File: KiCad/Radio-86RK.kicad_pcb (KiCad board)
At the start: 2 copper layers, 266.7 x 203.2 mm, 188 parts, among them J1 Video, J2 5V, J3 Power, J4 Cassette, J5 Serial, J6 Parallel, Q1 2N3904, Q2 2N3904, SW1 FF, SW10 ВК CR, SW11 ЗБ DEL, SW12 LEFT, SW13 UP, SW14 RIGHT, SW15 DOWN, SW16 0, SW17 1 !, SW18 2 ", SW19 3 #, SW2 СТР CLS, SW20 4 $, SW21 5 %, SW22 6 &, SW23 7 ', SW24 8 (, SW25 9 ), SW26 : *, SW27 ; +, SW28 , <, SW29 - =, SW3 АР2 ESC, SW30 . >, SW31 / ?, SW32 Ю @, SW33 А A, SW34 Б B, SW35 Ц C, SW36 Д D, SW37 Е E, SW38 Ф F, SW39 Г G, SW4 F1, SW40 Х H, SW41 И I, SW42 Й J, SW43 К K, SW44 Л L, SW45 М M, SW46 Н N, SW47 О O, SW48 П P, SW49 Я Q, SW5 F2, SW50 Р R, SW51 С S, SW52 Т T, SW53 У U, SW54 Ж V, SW55 В W, SW56 X Ь, SW57 Ы Y, SW58 З Z, SW59 Ш [, SW6 F3, SW60 Э \, SW61 Щ ], SW62 Ч ^, SW63 SPACE, SW64 УС CTRL, SW65 CC GRAPH, SW66 RUS/LAT, SW67 Reset, SW7 F4, SW8 ТАБ TAB, SW9 ПС LF, U1 8080A/КР580ВМ80А, U10 2716/КР573РФ5, U11 2716/КР573РФ5, U12 74LS373/К555ИР22, U13 74198/К155ИР13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

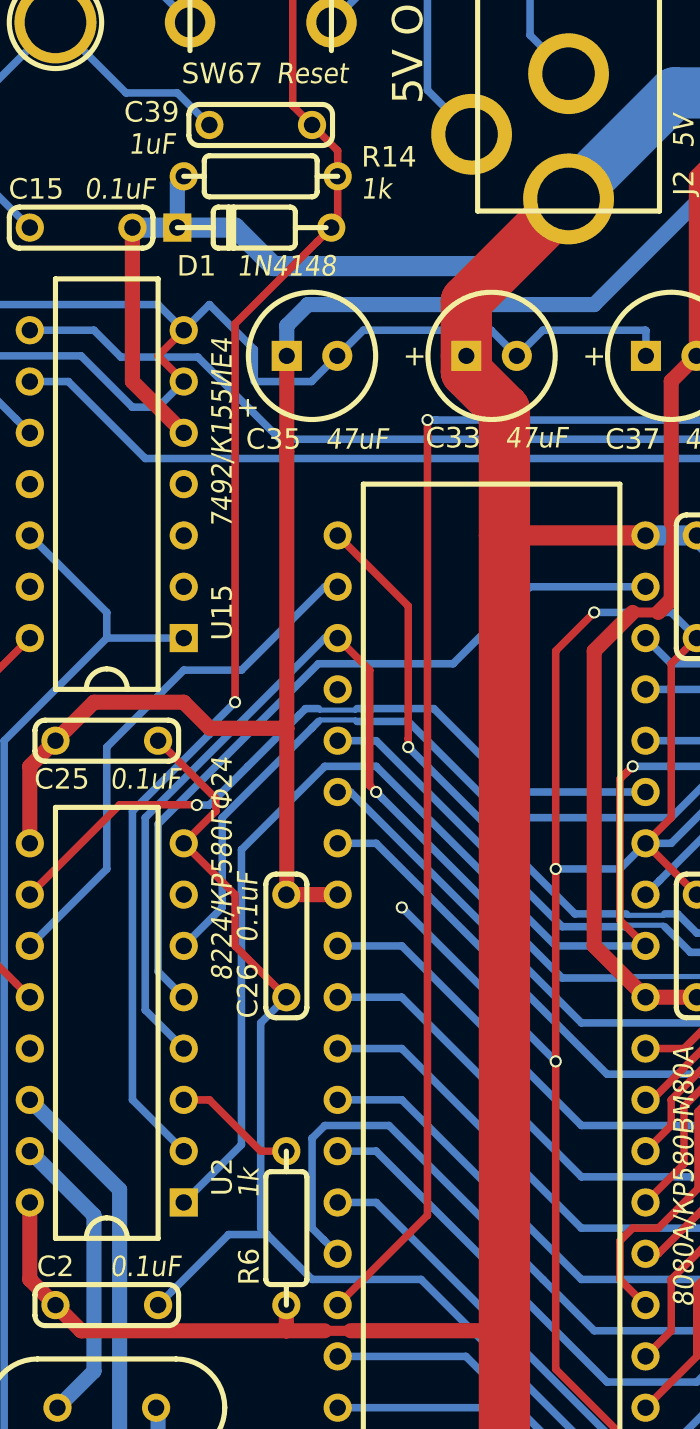
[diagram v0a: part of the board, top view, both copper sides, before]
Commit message: Use DS1233 for reset
Signed-off-by: Sergey Kiselev <skiselev@gmail.com>
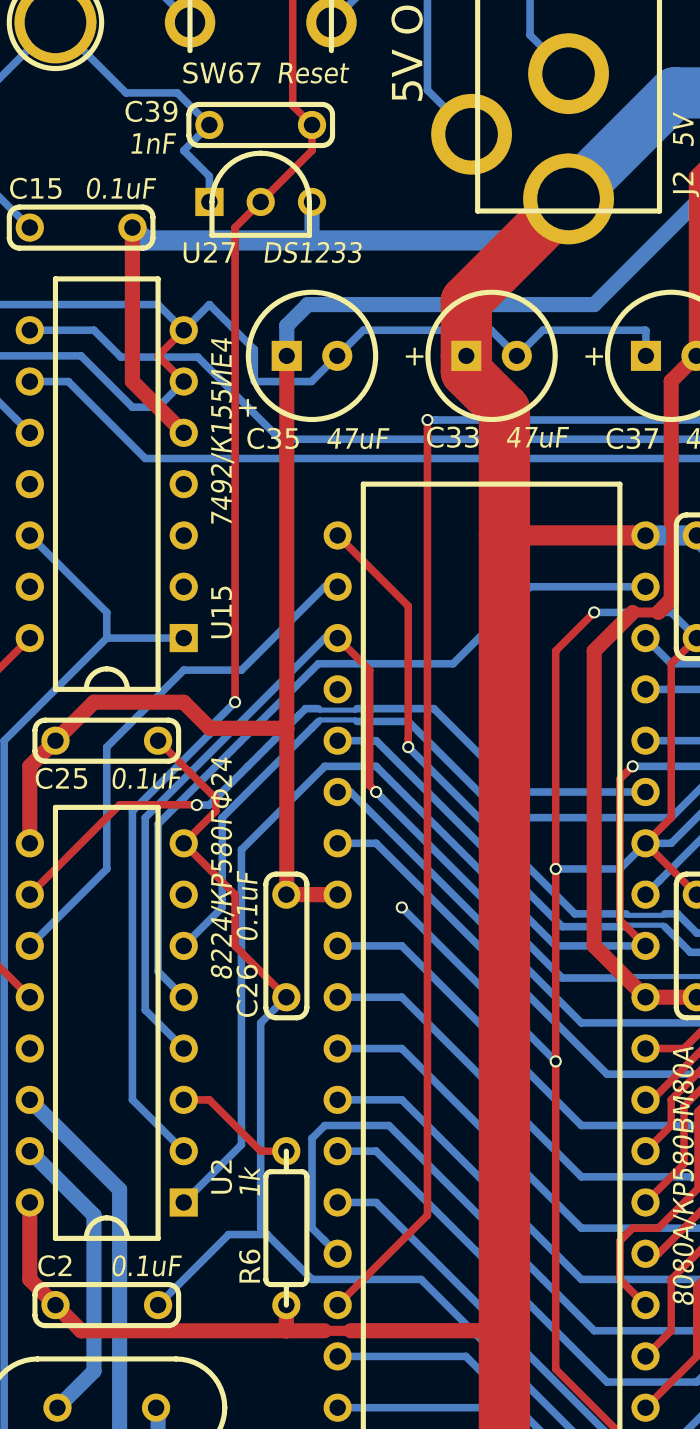
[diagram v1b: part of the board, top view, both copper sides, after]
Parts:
- removed D1: 1N4148, My_Components:Diode_762
- removed R14: 1k, My_Components:Res_762
- added U27: DS1233, My_Components:Transistor_TO92_EBC_254, F.Cu at (21.6, 20.3)
- C39: value 1uF -> 1nF
- turned R6 to 270 degrees
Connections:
- R6 pad 1: VCC -> Net-(R6-Pad1)
- R6 pad 2: Net-(R6-Pad2) -> VCC
- U2 pad 3: Net-(R6-Pad2) -> Net-(R6-Pad1)
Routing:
- net Net-(R6-Pad2): track 6.13 -> 0.00 mm
- net Net-(R6-Pad1): track 0.00 -> 6.13 mm
- net GND: track 2983.2 -> 2988.1 mm
- net VCC: track 1026.8 -> 1025.0 mm
- net Net-(C39-Pad1): track 64.8 -> 63.8 mm

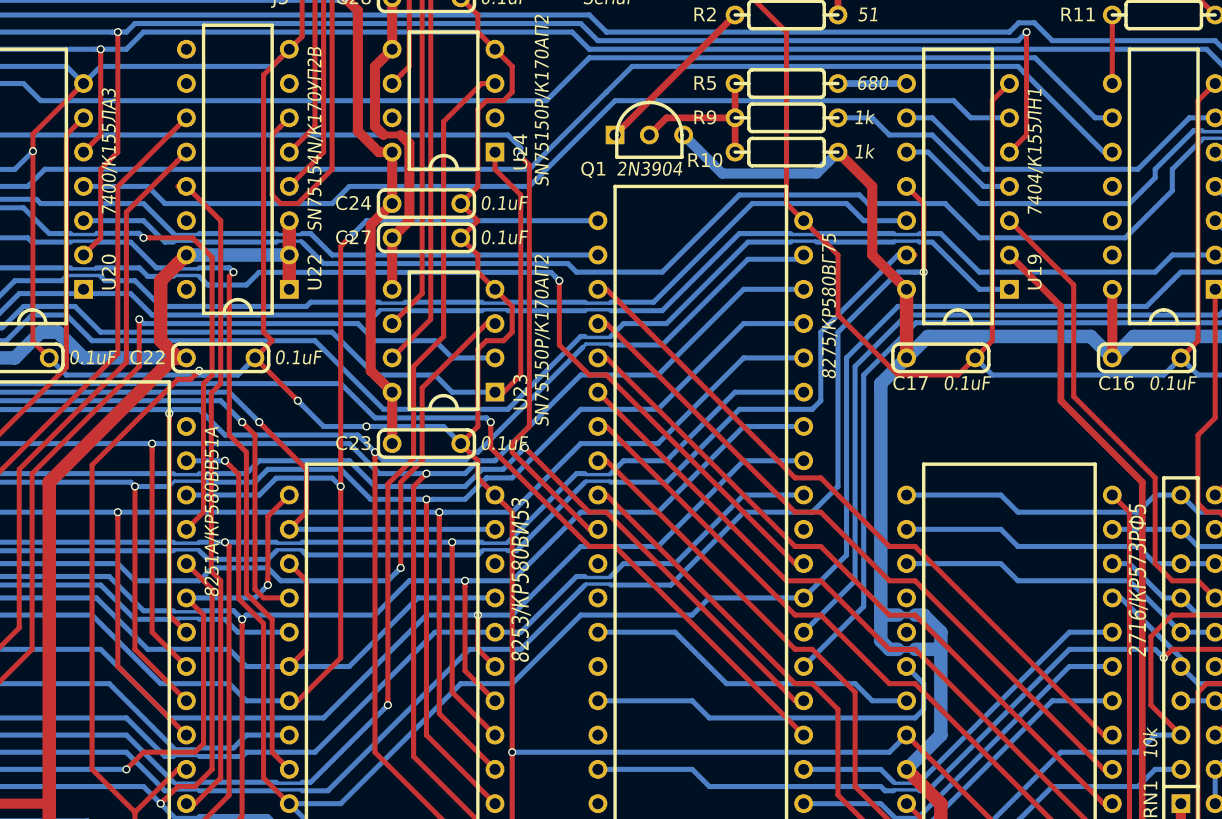
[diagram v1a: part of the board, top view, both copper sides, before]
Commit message: Implement inverse video
Signed-off-by: Sergey Kiselev <skiselev@gmail.com>
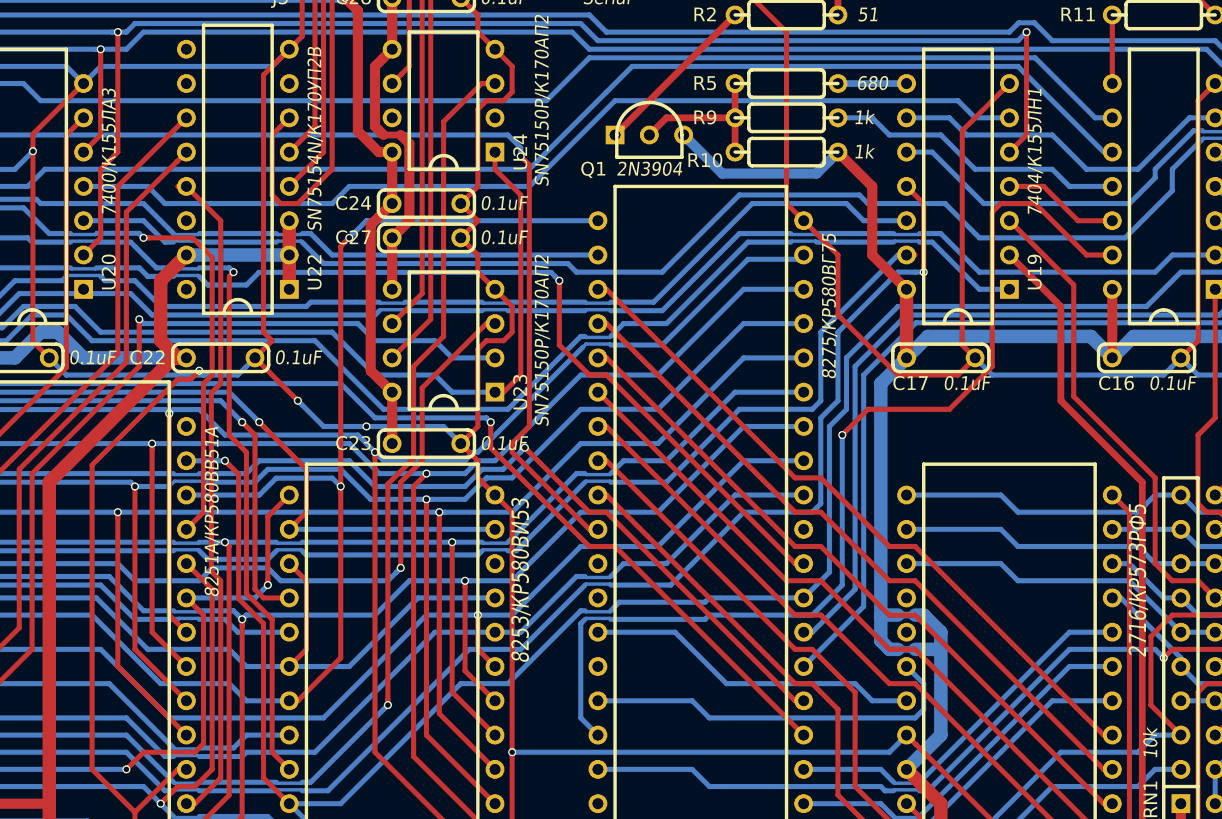
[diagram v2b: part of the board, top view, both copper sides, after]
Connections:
- U16 pad 11: Net-(U16-Pad11) -> Net-(R9-Pad2)
- U19 pad 4: Net-(R9-Pad2) -> Net-(U16-Pad12)
- U8 pad 36: Net-(U8-Pad36) -> Net-(U16-Pad13)
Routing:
- net Net-(U16-Pad13): track 0.00 -> 75.9 mm, vias 0 -> 1
- net Net-(U16-Pad12): track 0.00 -> 8.67 mm
- net Net-(R9-Pad2): track 14.8 -> 22.4 mm
- net GND: track 2988.1 -> 2988.9 mm

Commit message: Update design files to v1.1
Signed-off-by: Sergey Kiselev <skiselev@gmail.com>
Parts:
- removed the C39 at (21.6, 16.5)
- added C43: 1nF, My_Components:Cap_Cer_508, F.Cu at (21.6, 16.5)
- renumbered C40 to C39, C41 to C40, C42 to C41, C43 to C42, D2 to D1, D11 to D10, D12 to D11, D3 to D2, D4 to D3, D5 to D4, D6 to D5, D7 to D6, D8 to D7, D9 to D8, D10 to D9, R15 to R14, R16 to R15
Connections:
- D10 pad 2: /Keyboard/D11+ -> /Keyboard/D10+
- D11 pad 2: /Keyboard/D12+ -> /Keyboard/D11+
- R12 pad 2: /Keyboard/D11+ -> /Keyboard/D10+
- R13 pad 2: /Keyboard/D12+ -> /Keyboard/D11+
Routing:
- net /Keyboard/D10+: track 0.00 -> 15.0 mm
- net /Keyboard/D12+: track 8.30 -> 0.00 mm
- net /Keyboard/D11+: track 15.0 -> 8.30 mm
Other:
- board text added: "M<Address> - Modify memory content T<Start_Address>,<End_Address>,<Destination_Start_Address> - Copy memory block to destination C<Start_Address>,<End_Address>,<Destination_Start_Address> - Compare memory block with destination S<Start_Address>,<End_Address>,<Value> - Search memory for a value"
- board text added: "R<ROM_Start_Address>,<ROM_End_Address>,<Destination_Start_Address> - Read from ROM connected to Parallel interface to memory Monitor Commands - Run Control and Registers: G<Start_Address>[,End_Address] - Run code, optionally stop at the specified address X - Display and modify registers"
- board text added: "Radio-86RK - Version 1.1 PCB Layout - Copyright (C) Sergey Kiselev github.com/skiselev/radio-86rk"
- board text removed: "Monitor Commands - Run Control and Registers: G<Start_Address>[,End_Address] - Run code, optionally stop at the specified address X - Display and modify registers"
- board text removed: "Radio-86RK - Version 1.0 PCB Layout - Copyright (C) Sergey Kiselev github.com/skiselev/radio-86rk"
- board text removed: "T<Start_Address>,<End_Address>,<Destination_Start_Address> - Copy memory block to destination C<Start_Address>,<End_Address>,<Destination_Start_Address> - Compare memory block with destination S<Start_Address>,<End_Address>,<Value> - Search memory for a value R<ROM_Start_Address>,<ROM_End_Address>,<Destination_Start_Address> - Read from ROM connected to Parallel interface to memory"

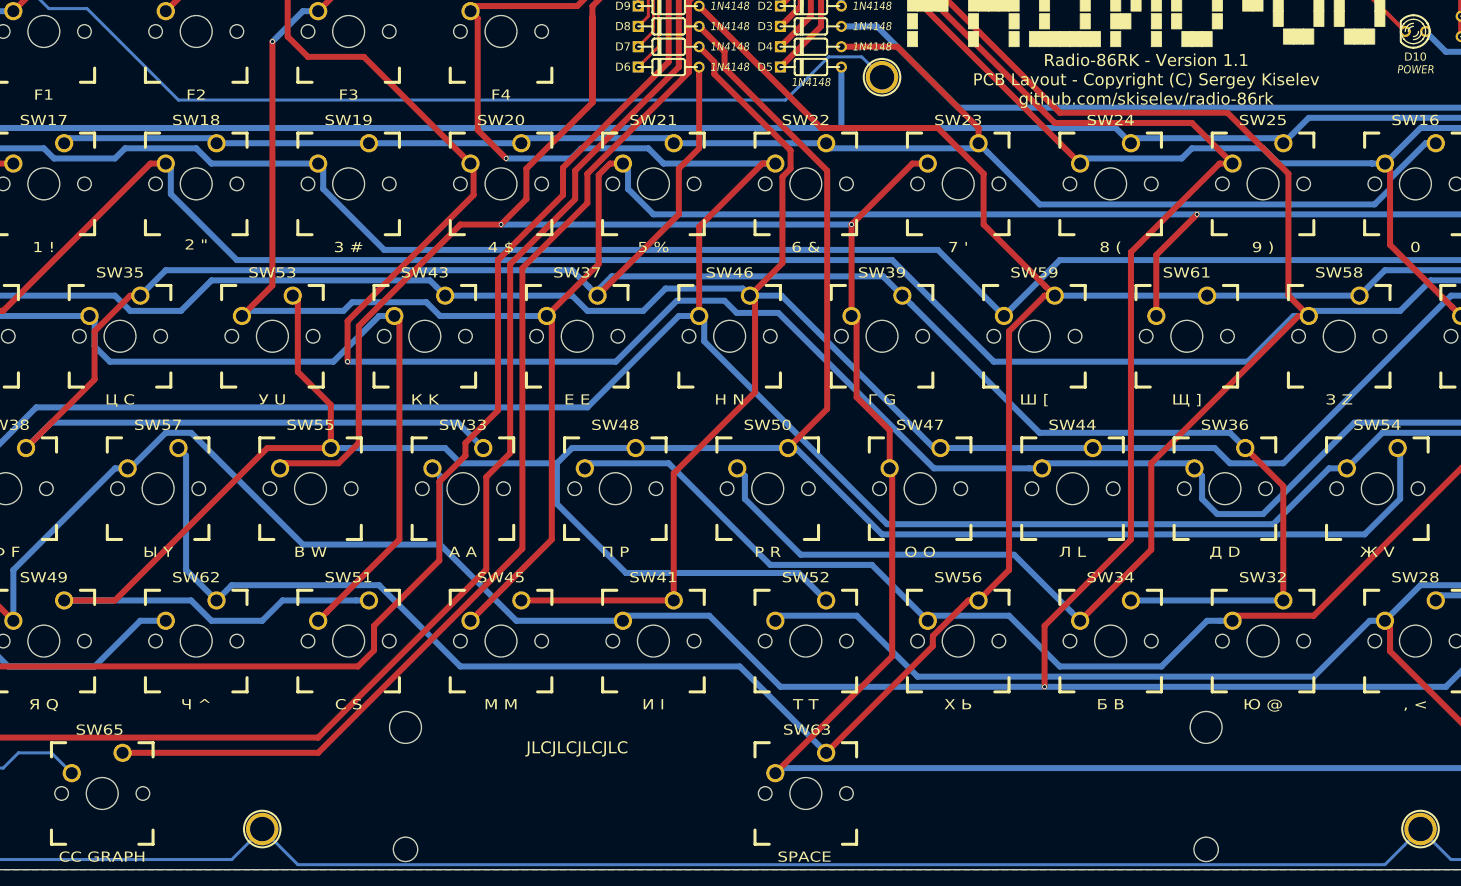
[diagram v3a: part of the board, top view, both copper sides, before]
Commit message: Fix issues on the front silkscreen
Signed-off-by: Sergey Kiselev <skiselev@gmail.com>
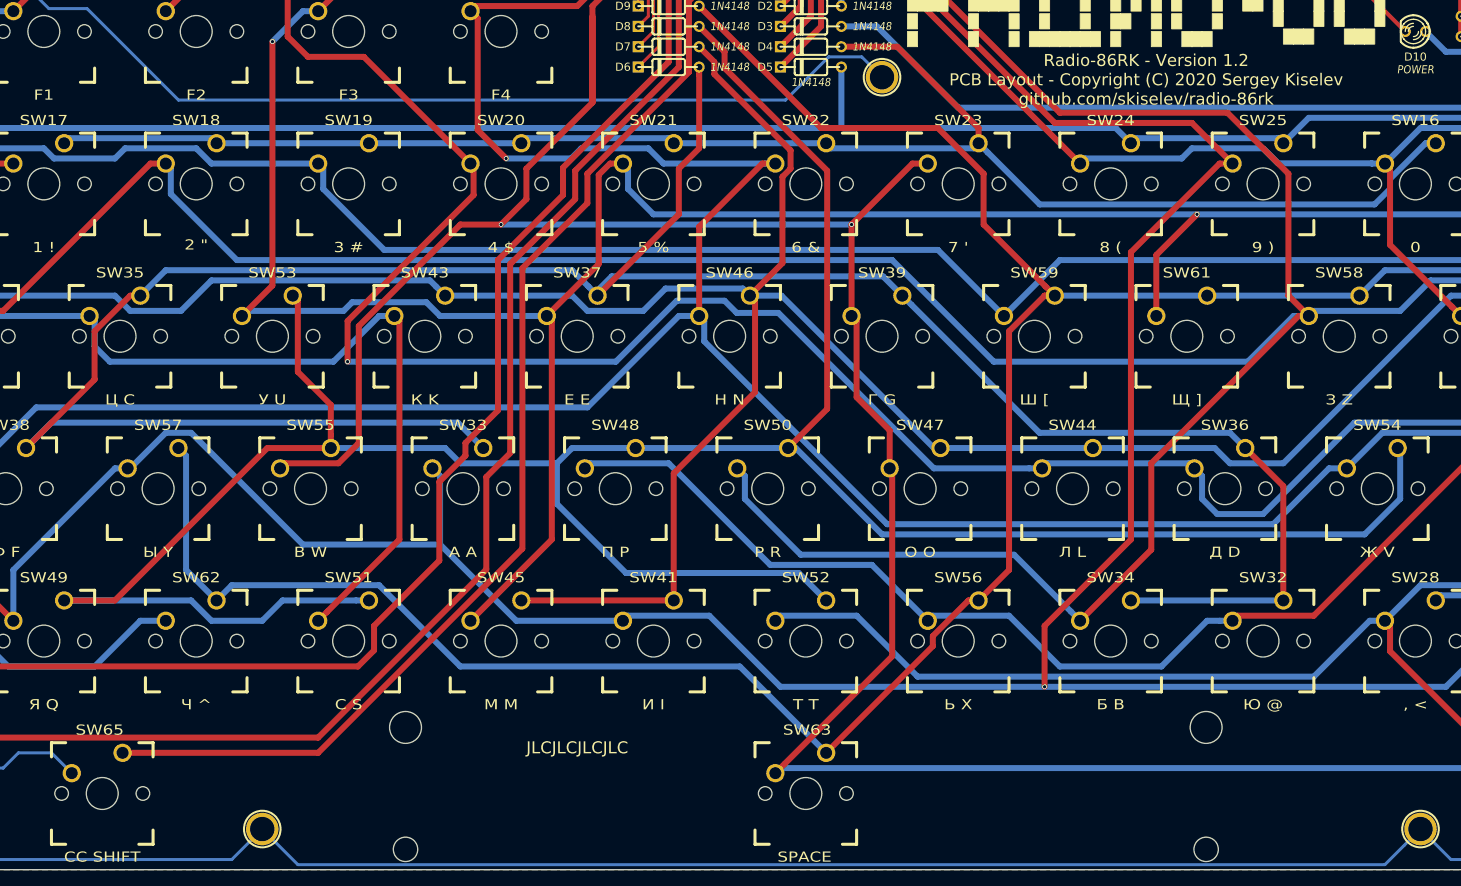
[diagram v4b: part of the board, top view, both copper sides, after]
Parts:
- SW56: value X Ь -> Ь X
- SW65: value CC GRAPH -> CC SHIFT
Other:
- board text added: "Radio-86RK - Version 1.2 PCB Layout - Copyright (C) 2020 Sergey Kiselev github.com/skiselev/radio-86rk"
- board text removed: "Radio-86RK - Version 1.1 PCB Layout - Copyright (C) Sergey Kiselev github.com/skiselev/radio-86rk"
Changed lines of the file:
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@@
     (35 F.Paste user)
     (36 B.SilkS user)
-    (37 F.SilkS user)
+    (37 F.SilkS user hide)
     (38 B.Mask user)
     (39 F.Mask user)
@@
       (effects (font (size 1.27 1.524) (thickness 0.2032)))
     )
-    (fp_text value "X Ь" (at 0 7.9375) (layer F.SilkS)
+    (fp_text value "Ь X" (at 0 7.9375) (layer F.SilkS)
       (effects (font (size 1.27 1.524) (thickness 0.2032)))
     )
@@
       (effects (font (size 1.27 1.524) (thickness 0.2032)))
     )
-    (fp_text value "CC GRAPH" (at 0 7.9375) (layer F.SilkS)
+    (fp_text value "CC SHIFT" (at 0 7.9375) (layer F.SilkS)
       (effects (font (size 1.27 1.524) (thickness 0.2032)))
     )
@@
     (effects (font (size 1.5 1.5) (thickness 0.2)) (justify left mirror))
   )
-  (gr_text "R<ROM_Start_Address>,<ROM_End_Address>,<Destination_Start_Address> - Read from ROM connected to Parallel interface to  memory\nMonitor Commands - Run Control and Registers:\nG<Start_Address>[,End_Address] - Run code, optionally stop at the specified address\nX - Display and modify registers" (at 236.5375 169.2275) (layer B.SilkS)
+  (gr_text "R<ROM_Start_Address>,<ROM_End_Address>,<Destination_Start_Address> - Read from ROM connected to Parallel interface to memory\nMonitor Commands - Run Control and Registers:\nG<Start_Address>[,End_Address] - Run code, optionally stop at the specified address\nX - Display and modify registers" (at 236.5375 169.2275) (layer B.SilkS)
     (effects (font (size 1.5 1.5) (thickness 0.2)) (justify left mirror))
   )
@@
     (effects (font (size 1 1) (thickness 0.15)) (justify left mirror))
   )
-  (gr_text "Radio-86RK - Version 1.1\nPCB Layout - Copyright (C) Sergey Kiselev\ngithub.com/skiselev/radio-86rk" (at 172.72 110.8075) (layer F.SilkS)
+  (gr_text "Radio-86RK - Version 1.2\nPCB Layout - Copyright (C) 2020 Sergey Kiselev\ngithub.com/skiselev/radio-86rk" (at 172.72 110.8075) (layer F.SilkS)
     (effects (font (size 1.5 1.5) (thickness 0.2)))
   )
